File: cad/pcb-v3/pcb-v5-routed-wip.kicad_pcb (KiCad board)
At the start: 4 copper layers, 20 x 19 mm, 50 parts

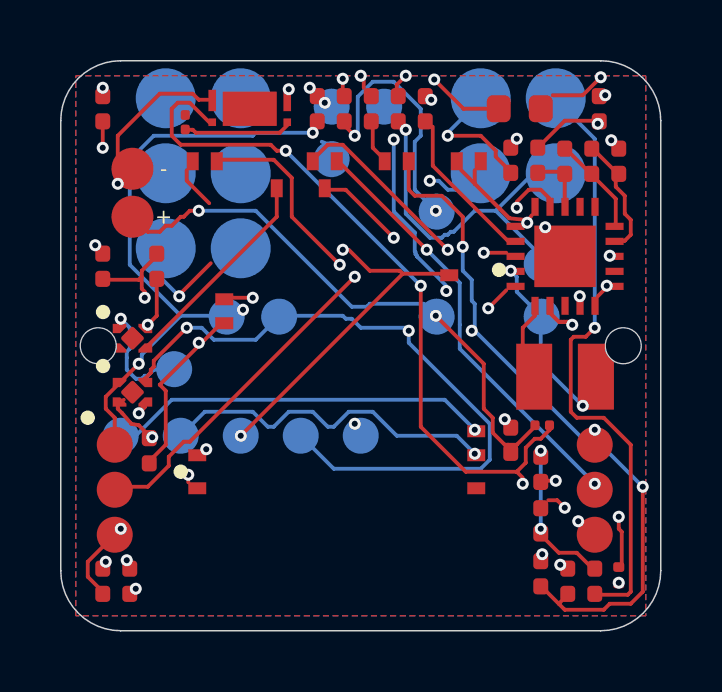
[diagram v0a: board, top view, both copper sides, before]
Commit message: VBAT to stage 1, fix the ROV2 clearance: clearance 0, DRC phantom-only
VBAT promoted to stage 1. U2.18 could reach 24712 cells and 2748 via sites --
it was never boxed in -- but NONE of that region touched any VBAT copper: the
net was split into two pieces that never met. Routing it early fixes the split
at source. Stage 1 is now 12/12 single-ended and 17/17 multi-point pads.

Fixed a real 0.0085 mm shortfall: ROV2.1 (VRDIV) sat 0.0915 from a VBAT_OV_SET
track where the rule is 0.100 -- the divider's own routing passing its other
pad. --routing-clearance-margin did not help, so the offending vertical
segment moved 0.030 mm clear, with all four coincident endpoints moved
together so nothing came apart.

check_board: 0 clearance violations.
check_drc: 5, ALL PHANTOM. Every one cites a 'Via:GND' at (2.90,-7.00); the
file has exactly ONE via there, net 5, and the table says net 5 = HARV_1 with
GND on net 4. check_drc is mis-resolving net numbers -- same class of defect
as its pad-rotation bug. Not acting on them.

Board is UNFILLED again after the re-route.
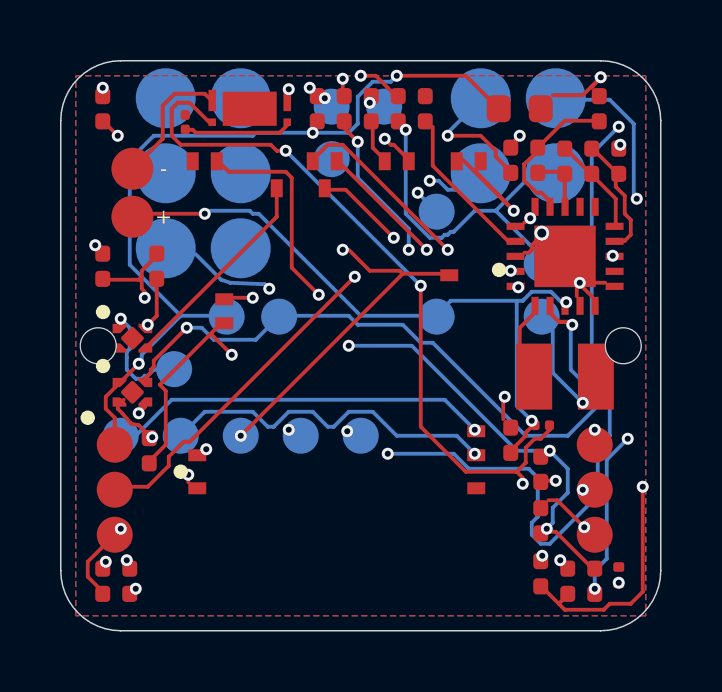
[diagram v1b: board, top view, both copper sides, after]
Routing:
- net BL_FLAG: track 22.5 -> 50.4 mm, vias 3 -> 5
- net CELL_NEG: track 29.6 -> 4.42 mm, vias 2 -> 0
- net VIN_DC: track 23.9 -> 46.0 mm, vias 5 -> 6
- net SENSOR_3V3: track 37.9 -> 28.0 mm, vias 6 -> 3
- net VBAT_OV_SET: track 10.3 -> 5.19 mm, vias 2 -> 0
- net VSTOR: track 68.8 -> 72.2 mm, vias 9 -> 8
- net VBAT: track 19.2 -> 22.3 mm, vias 2 -> 3
- net VBAT_OK: track 29.2 -> 27.1 mm, vias 4 -> 5
- net VBAT_SENSE: track 12.3 -> 13.8 mm
- net SENSOR_RX: track 14.6 -> 15.8 mm
- net GND: track 16.3 -> 16.2 mm, vias 28 -> 24
- net HARV_2: track 20.2 -> 20.3 mm, vias 1 -> 3

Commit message: wire up the PCM cluster constraint that was written but never read
C14 -- the PCM's supply bypass -- was 19.77 mm from U5 on a 20 mm board. Three
things were wrong, all of them latent:

1. SMALL_NEAR = (3.0, 4.5, 6.0, 8.0) existed, and _place_smalls' own comment
   said 'keep them within SMALL_NEAR of U5', but NOTHING EVER READ IT.
   Distance only ever RANKED candidates; it never REJECTED one. With the shelf
   beside U5 full, 'nearest' became the far corner.
2. CLUSTER_OK was 99.0 -- the guard meant to reject a U5 position that
   scatters its cluster was effectively switched off.
3. _place_smalls masked every 0402 SLOT out and hunted leftover space, while
   its own docstring said these parts take slots. There is no leftover space
   next to U5, which is why forcing a radius made every U5 trial fail outright.

Fixed: per-part ladders (C14 tightest, it is the bypass; R8 loosest, its 330
ohm swamps any parasitic), C14 placed FIRST so it takes the best spot rather
than the leftovers, CLUSTER_OK 99 -> 8, and slot centres offered as candidates
with the consumed slot handed back to the packer. Slot candidates are checked
against the real legality mask -- skipping that first put R8 past the 17.94
housing cavity and overlapped C14 with R9.

    C14  19.77 mm -> 3.42     R8  14.31 -> 4.75     R9  2.18 -> 1.95

Routing: PCM_VDD then CELL_NEG then PCM_VM must go BEFORE the rest of stage 1.
With the cluster tight, PCM_VM takes the corridor PCM_VDD needs to reach C14
and PCM_VDD fails. Split into stage 1a (PCM) and 1b (the rest); all route.

New push_off_pads.py: the router lays copper 1-9 microns inside the clearance
rule against ROTATED 0402 pads, on a different net every re-route. Hand-nudging
one segment at a time had been done twice. This finds every grazing track,
computes the shortest perpendicular push, and RE-TESTS the pushed segment
against every foreign pad, track and via before accepting it -- a fix that
trades one violation for another is not a fix. 28 segments p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
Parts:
- moved C14 20.7 mm to (-5.00, -7.90)
- moved R8 15.6 mm to (-8.60, -2.65), turned to 90 degrees
- moved R2 14.2 mm to (5.90, -6.18)
- moved C3 13.8 mm to (6.00, 5.84)
- moved R7 12.4 mm to (5.00, 3.15)
- moved C5 12.3 mm to (-0.50, -7.90)
- moved R5 10.5 mm to (-7.70, 7.85)
- moved C13 6.30 mm to (-2.30, -7.90)
- moved TP3 3.91 mm to (-0.97, -2.72)
- moved U5 3.55 mm to (-7.25, -7.90), turned to 180 degrees
- moved C1 2.70 mm to (7.80, 7.85)
- moved R9 1.81 mm to (-4.10, -7.90), turned to 0 degrees
- moved ROK3 1.77 mm to (7.05, -7.90)
- moved C10 0.93 mm to (6.00, 7.60)
- moved C2 0.93 mm to (6.90, 7.85)
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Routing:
- net BL_FLAG: track 50.4 -> 12.2 mm, vias 5 -> 3
- net VSTOR: track 72.2 -> 44.9 mm, vias 8 -> 5
- net PCM_VDD: track 28.7 -> 10.6 mm, vias 4 -> 0
- net VIN_DC: track 46.0 -> 32.6 mm
- net VBAT_OV_SET: track 5.19 -> 13.5 mm, vias 0 -> 2
- net GND: track 16.2 -> 8.12 mm, vias 24 -> 26
- net CELL_NEG: track 4.42 -> 10.2 mm
- net HARV_2: track 20.3 -> 14.7 mm, vias 3 -> 2
- net VREF_SAMP: track 5.23 -> 9.54 mm, vias 0 -> 3
- net VBAT_OK: track 27.1 -> 23.2 mm, vias 5 -> 4
- net VBAT: track 22.3 -> 25.8 mm, vias 3 -> 2
- net RESET: track 17.8 -> 14.4 mm
- net OK_HYST: track 3.41 -> 5.91 mm, vias 0 -> 2
- net SENSOR_WAKEUP: track 16.0 -> 13.5 mm
- net VBAT_SENSE: track 13.8 -> 16.2 mm, vias 2 -> 4
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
